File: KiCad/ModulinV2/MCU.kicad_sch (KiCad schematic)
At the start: 62 parts, among them IC2 STM32F401RET6, IC3 USBLC6-2SC6, J2 USB4105-GF-A, J3 TSM-103-01-T-DV, J4 TSW-104-07-G-S, Y1 CX2016FB24000B0FZZH1

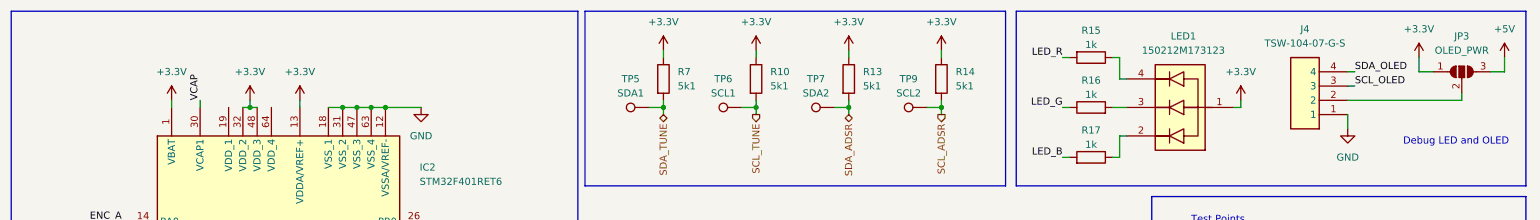
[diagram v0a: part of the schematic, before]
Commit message: Finished Schematic, started on PCB
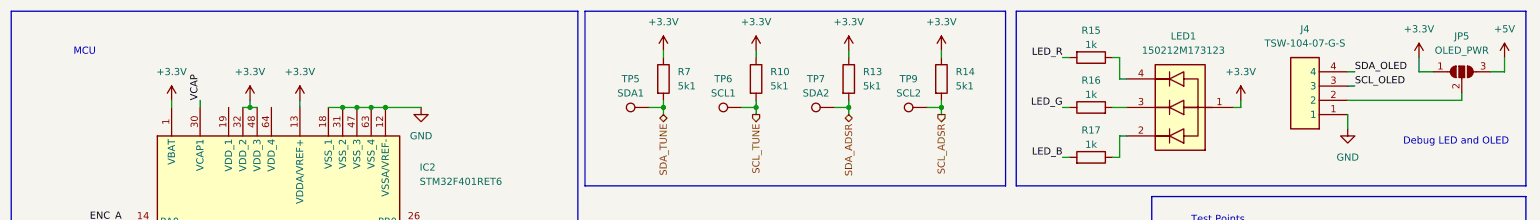
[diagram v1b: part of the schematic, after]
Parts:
- R10, R11, R12, R13, R14, R15, R16, R17, R5, R6, R7, R8, R9: footprint (none) -> Resistor_SMD:R_0603_1608Metric_Pad0.98x0.95mm_HandSolder
- renumbered JP3 to JP5
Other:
- note added: "MCU"

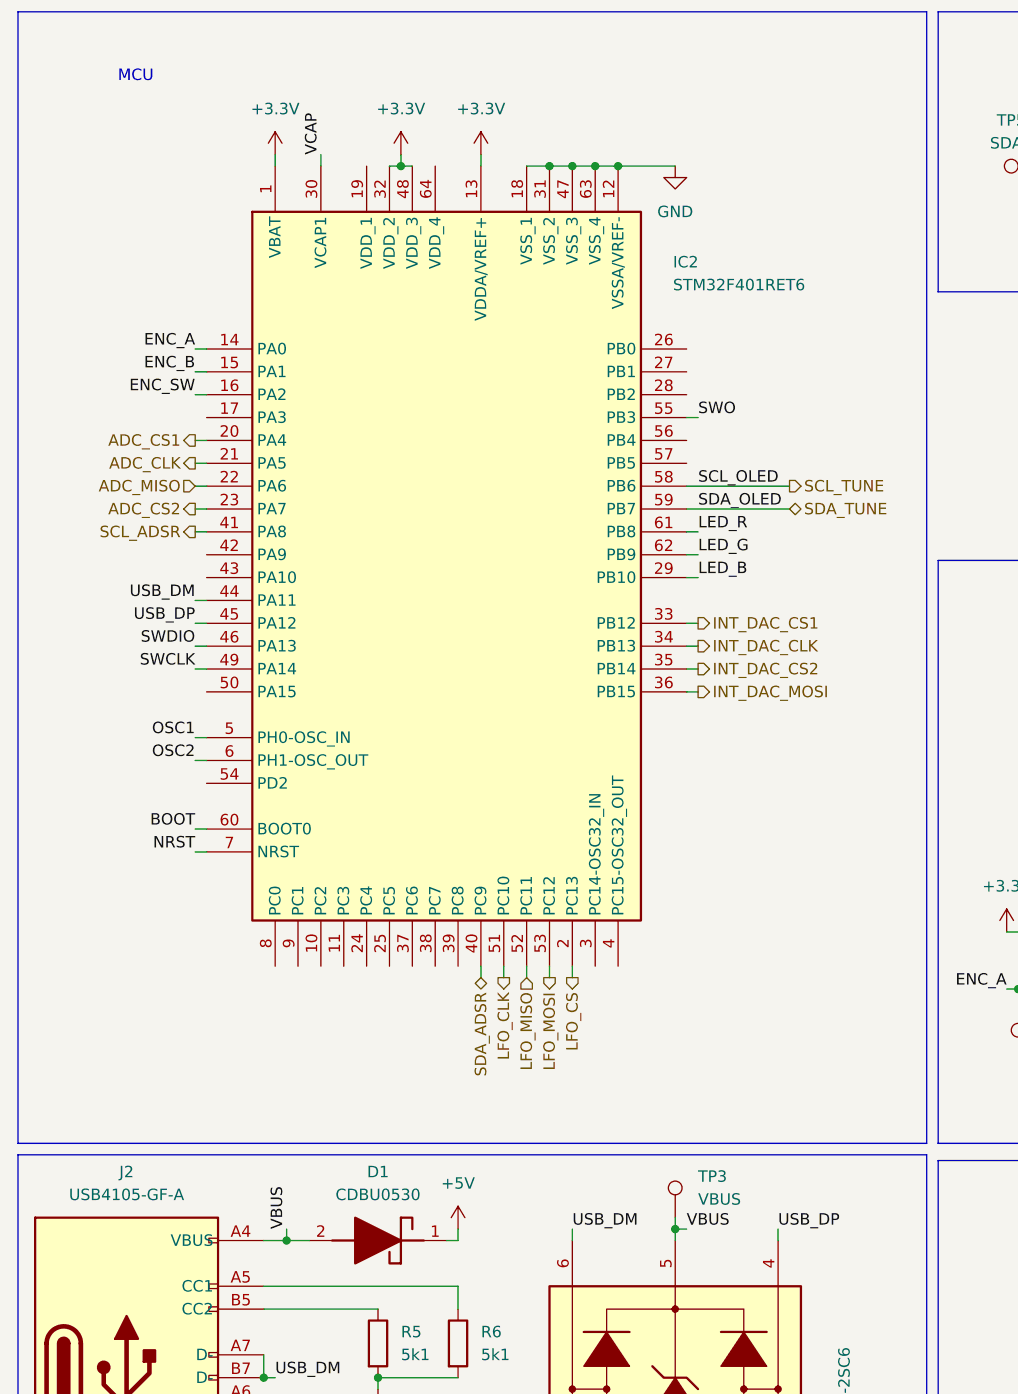
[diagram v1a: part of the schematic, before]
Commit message: Layed out Interface and PWR components and started with MCU layout
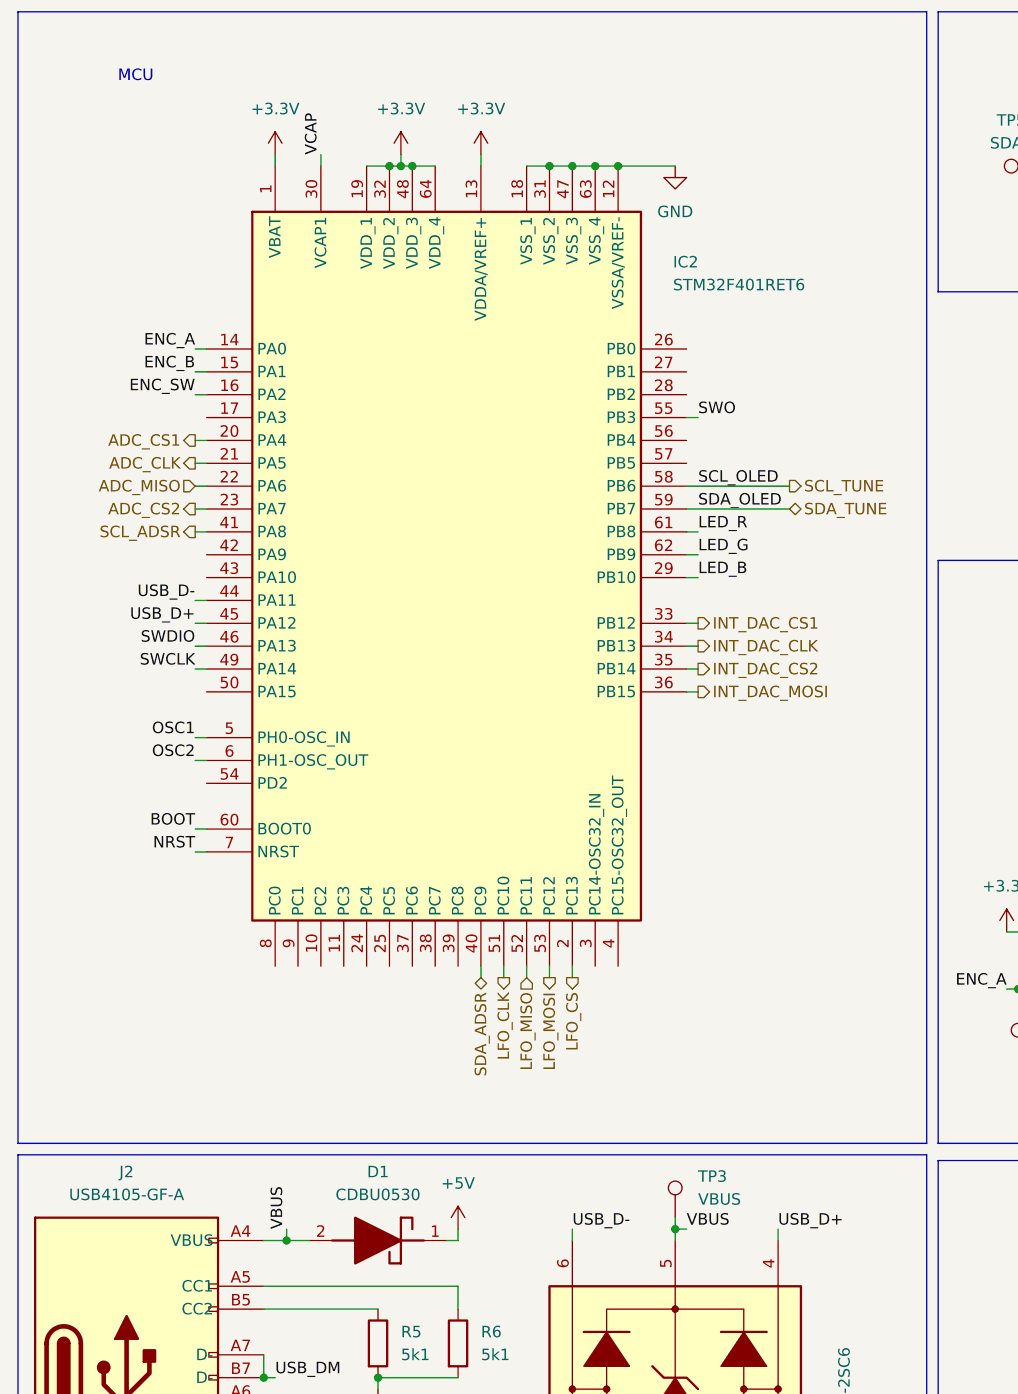
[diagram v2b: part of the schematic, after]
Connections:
- net +3.3V: now also IC2.19 (VDD_1), IC2.64 (VDD_4)
- net USB_DM: no longer IC2.44 (PA11), IC3.6
- net USB_DP: no longer IC2.45 (PA12), IC3.4
- new net USB_D+: IC2.45 (PA12), IC3.4
- new net USB_D-: IC2.44 (PA11), IC3.6

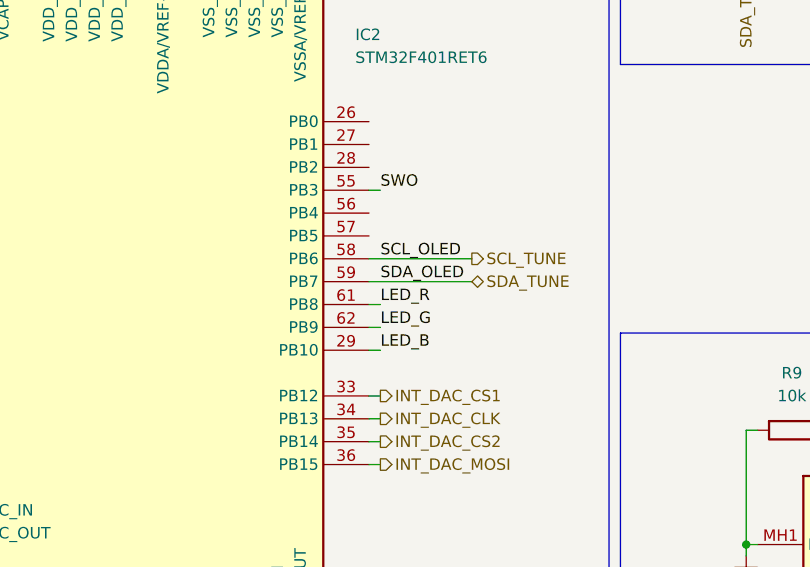
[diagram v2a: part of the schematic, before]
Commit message: Continued designing the MCU schematic
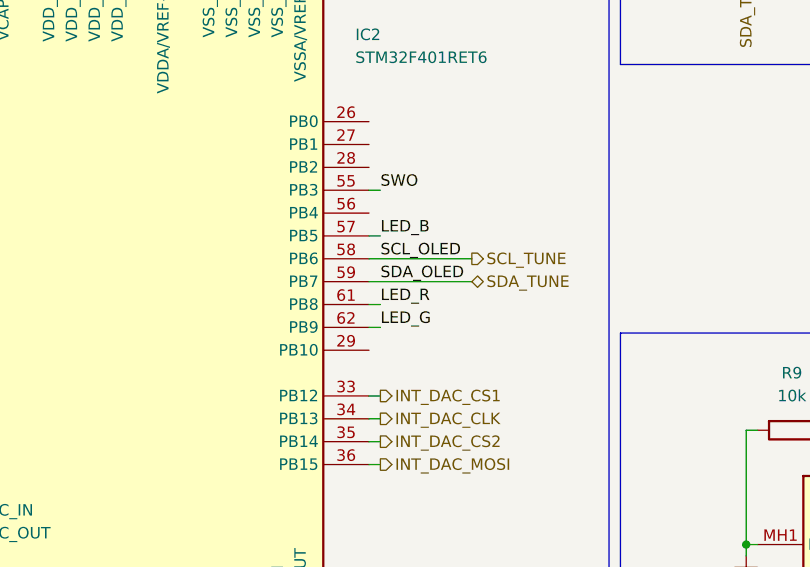
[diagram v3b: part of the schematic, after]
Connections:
- net LED_B: now also IC2.57 (PB5); no longer IC2.29 (PB10)
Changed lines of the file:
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@@
+	(wire
+		(pts
+			(xy 87.63 63.5) (xy 88.9 63.5)
+		)
+		(stroke
+			(width 0)
+			(type default)
+		)
+	)
 	(wire
 		(pts
@@
 		(pts
 			(xy 201.93 121.92) (xy 201.93 123.19)
-		)
-		(stroke
-			(width 0)
-			(type default)
-		)
-	)
-	(wire
-		(pts
-			(xy 87.63 76.2) (xy 88.9 76.2)
 		)
 		(stroke
@@
 	)
 	(label "LED_B"
-		(at 88.9 76.2 0)
+		(at 88.9 63.5 0)
 		(effects
 			(font

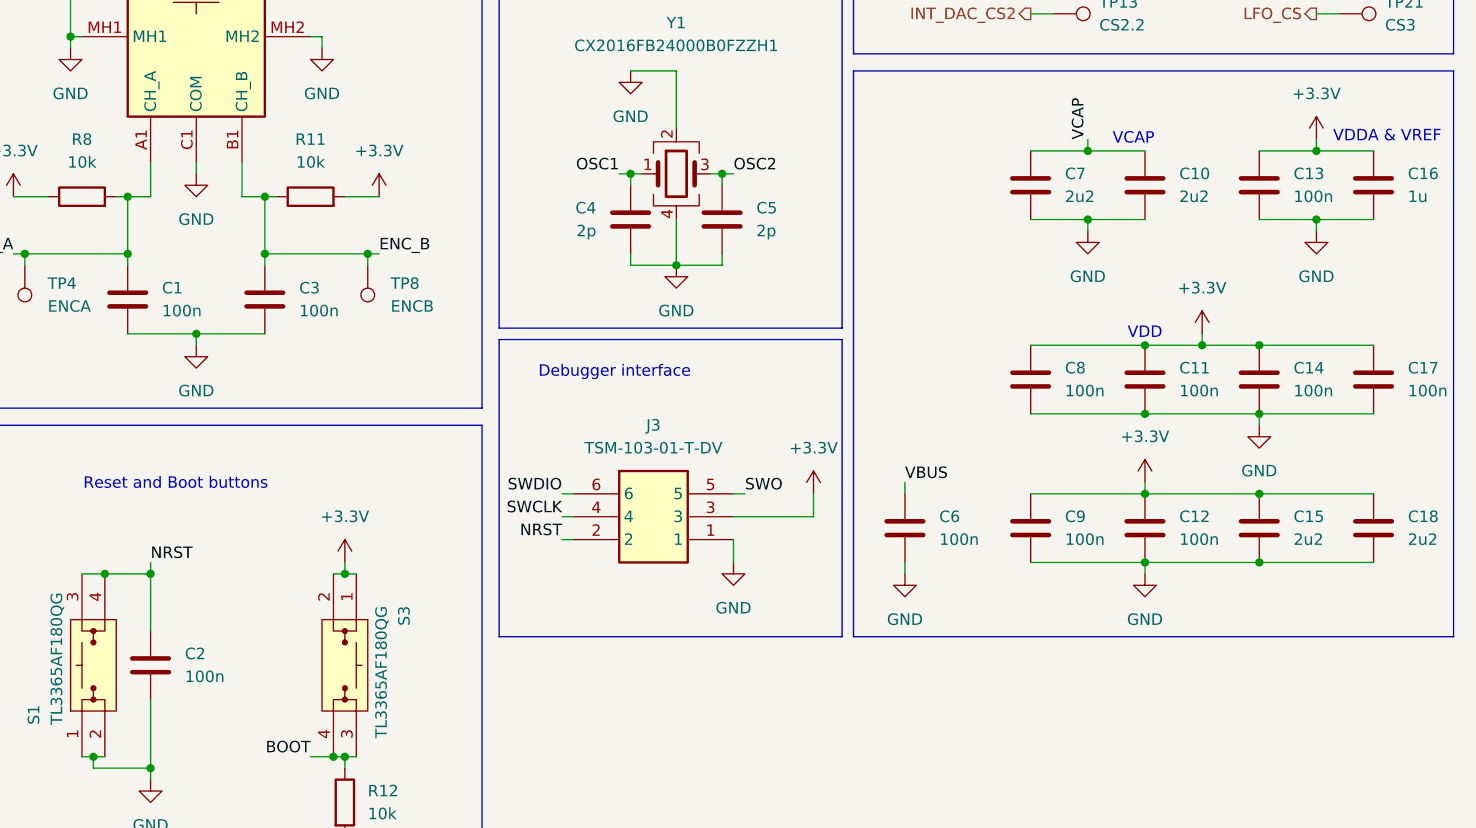
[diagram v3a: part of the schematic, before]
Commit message: Completed tuning & mod wheel layouts
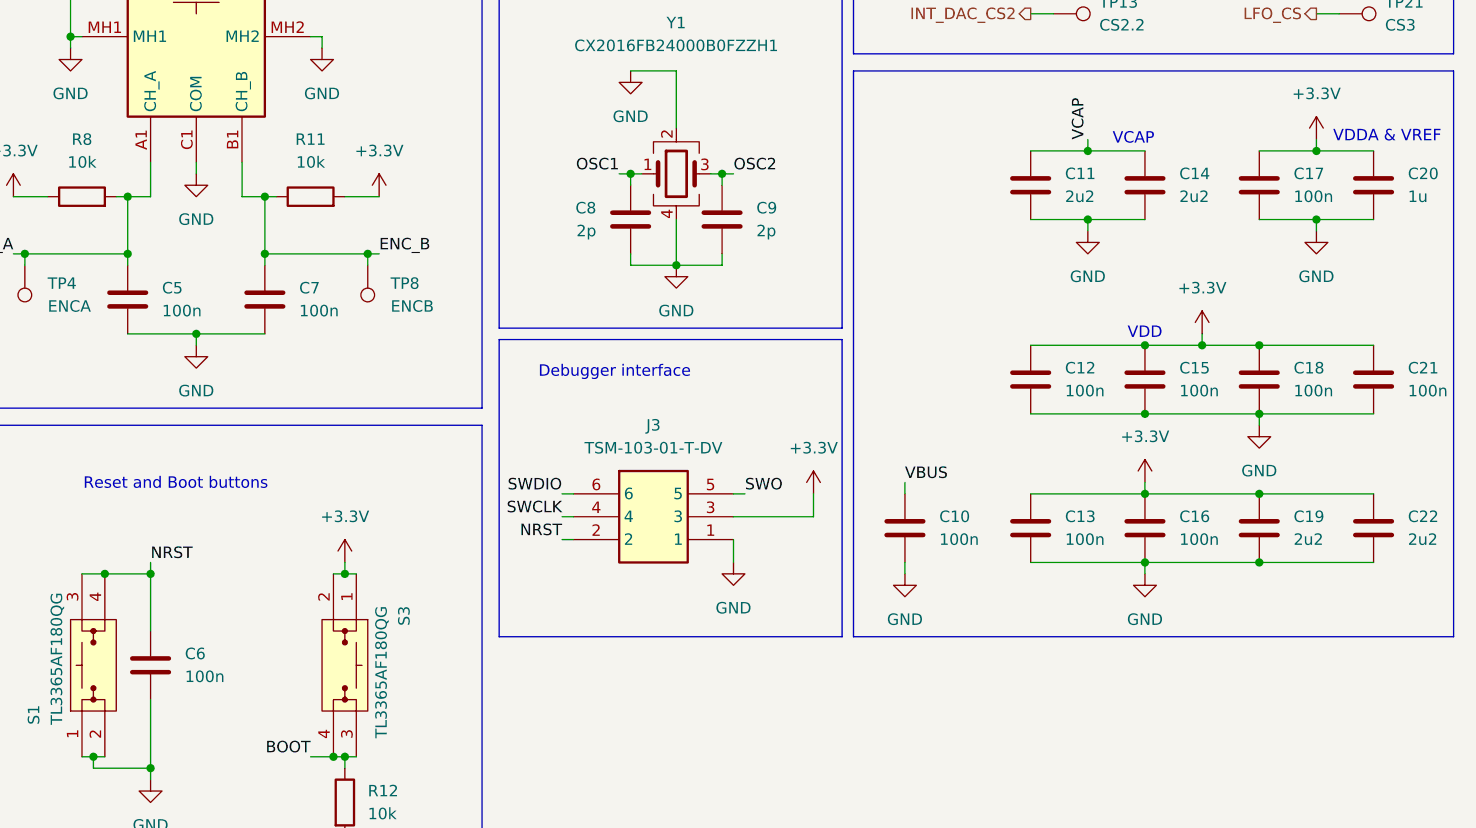
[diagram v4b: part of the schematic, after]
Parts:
- renumbered C6 to C10, C7 to C11, C8 to C12, C9 to C13, C10 to C14, C11 to C15, C12 to C16, C13 to C17, C14 to C18, C15 to C19, C16 to C20, C17 to C21, C18 to C22, C1 to C5, C2 to C6, C3 to C7, C4 to C8, C5 to C9

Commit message: Fixed schematic connections
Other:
- company: (none) -> TalTech
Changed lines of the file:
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@@
 	(title_block
 		(title "Microcontroller")
-		(date "2025-07-13")
-		(rev "1.0")
+		(date "2026-04-29")
+		(rev "1.4")
+		(company "TalTech")
 		(comment 1 "Instructor: Kaiser Pärnamets")
-		(comment 2 "By: Rasmus Palk")
+		(comment 2 "Author: Rasmus Palk")
 	)
 	(rectangle
